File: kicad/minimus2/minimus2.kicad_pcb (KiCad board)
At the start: 2 copper layers, 55.5 x 50 mm, 73 parts, among them J1 PROG_SER, J2 LM, J3 LM, Q1 SSM6N58NU_LF, Q2 SSM6N58NU_LF, Q3 DMN3051L, SW1 RESET, SW2 USER_A, SW3 USER_B, U1 LSM6DSRTR, U2 STM32U575CITx, U3 DRV8835, U4 AS5047D, U5 AS5047D, U6 BCR420UFD-7

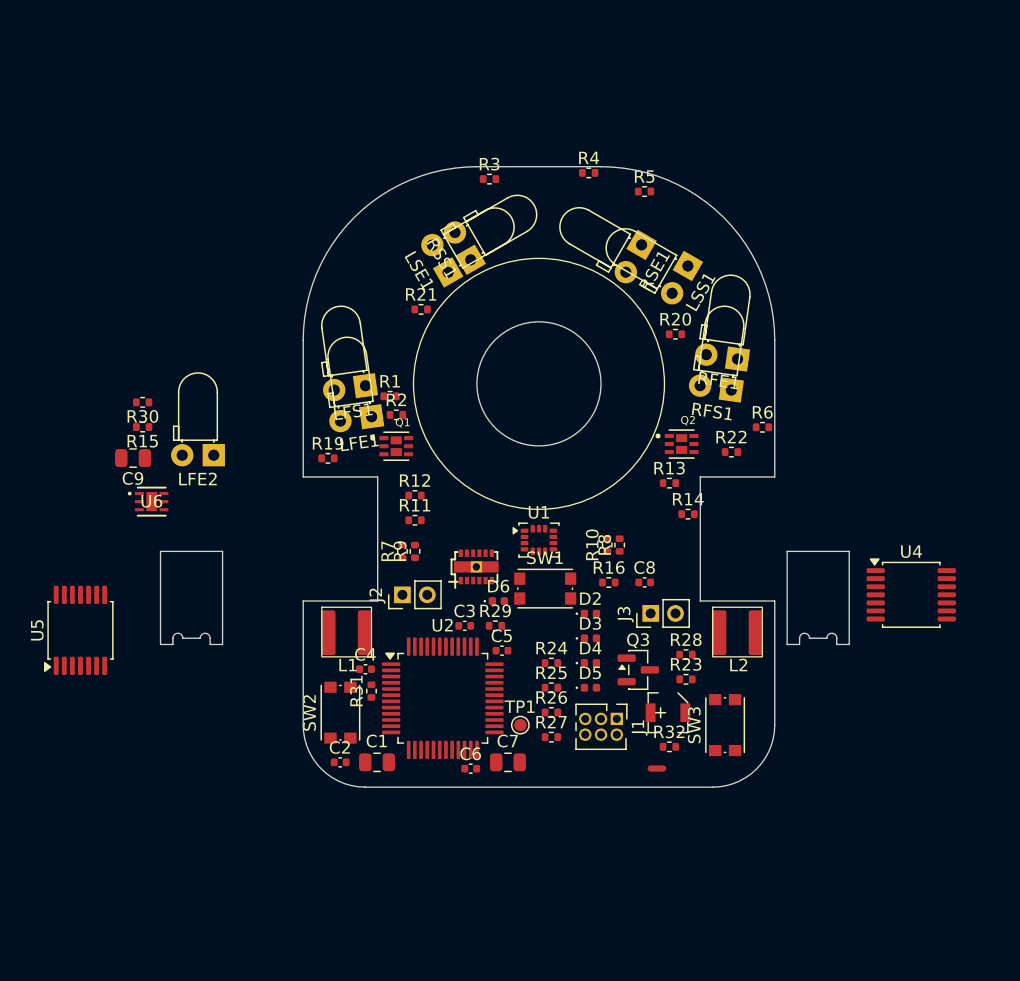
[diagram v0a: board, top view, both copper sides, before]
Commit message: remove unused switch and sensor
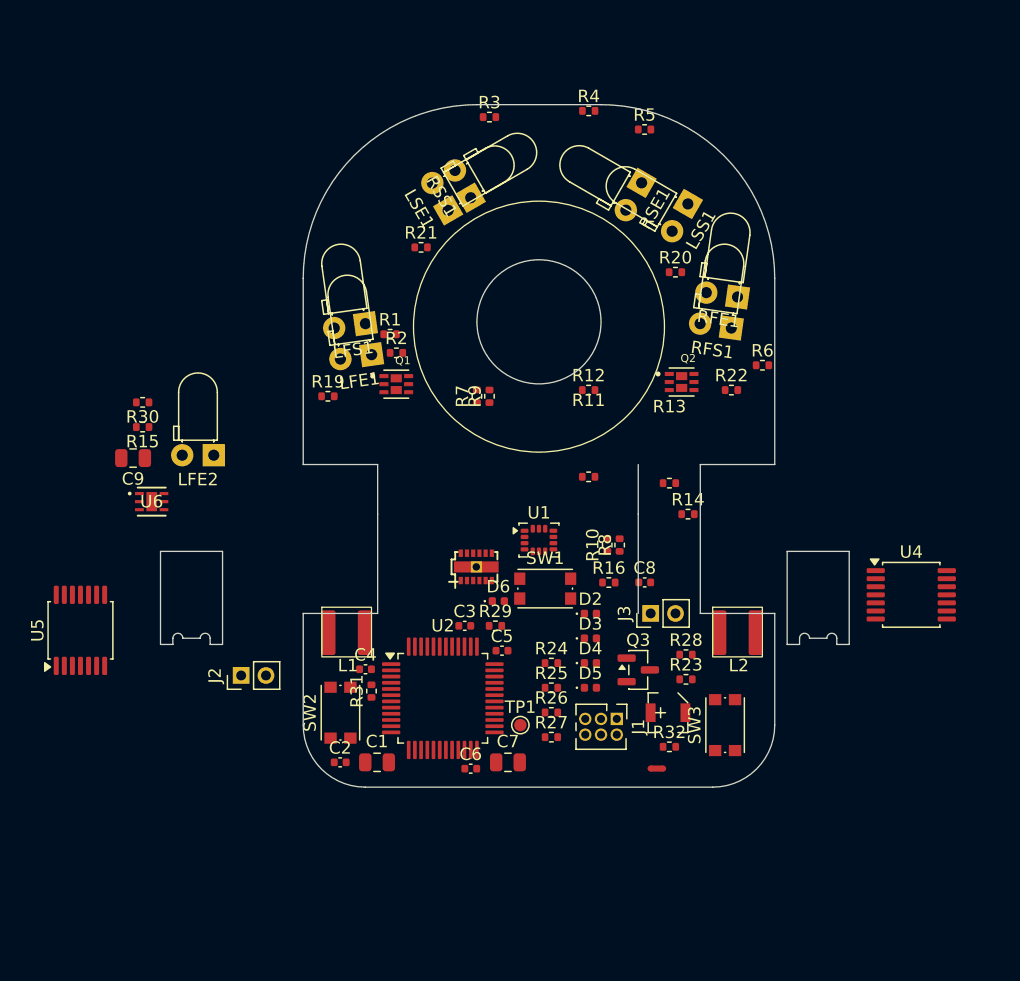
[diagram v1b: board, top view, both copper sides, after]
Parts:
- moved R12 16.4 mm to (104.0, 88.0)
- moved J2 14.5 mm to (76.0, 111.0)
- moved R11 14.4 mm to (104.0, 95.0)
- moved R7 13.9 mm to (95.0, 88.5)
- moved R9 13.9 mm to (96.0, 88.5)
- moved LFE1 5.00 mm to (86.5, 85.1)
- moved LFS1 5.00 mm to (86.0, 82.6)
- moved LSE1 5.00 mm to (92.7, 73.5)
- moved LSS1 5.00 mm to (112.0, 73.0)
- moved Q1 5.00 mm to (88.5, 87.5)
- moved Q2 5.00 mm to (111.5, 87.3)
- moved R1 5.00 mm to (88.0, 83.5)
- moved R19 5.00 mm to (83.0, 88.5)
- moved R2 5.00 mm to (88.5, 85.0)
- moved R20 5.00 mm to (111.0, 78.5)
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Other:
- board size 55.5 x 50 mm -> 55.5 x 55 mm

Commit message: add regulators and rotate board
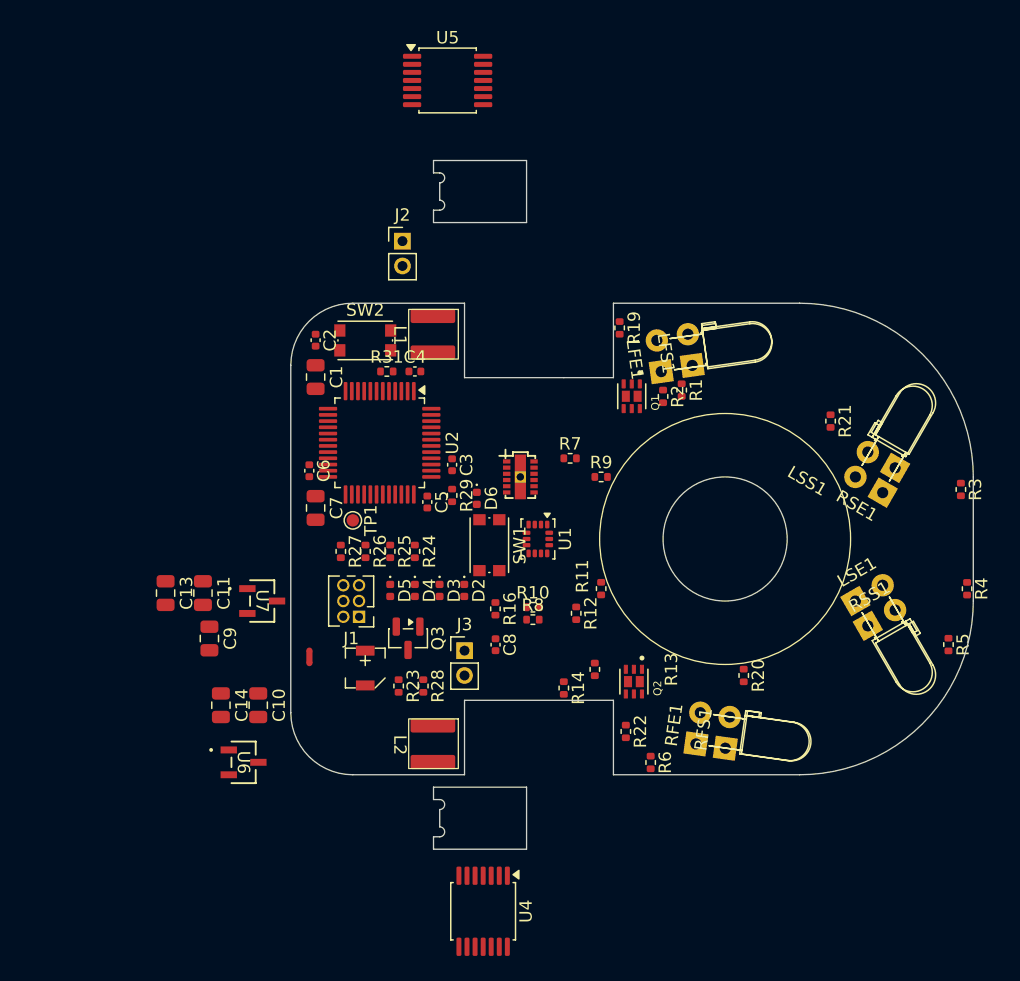
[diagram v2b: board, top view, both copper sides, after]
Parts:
- removed LFE2: SFH4050, LED_THT:LED_D3.0mm_Horizontal_O1.27mm_Z2.0mm_IRBlack
- removed R15, R30: 5k6, Resistor_SMD:R_0402_1005Metric
- removed R32: 47k, Resistor_SMD:R_0402_1005Metric
- removed SW3: USER_B, Button_Switch_SMD:SW_Push_1P1T_NO_CK_KMR2
- added C10: 4.7uF, Capacitor_SMD:C_0805_2012Metric, F.Cu at (77.4, 113.4)
- added C11: 4.7uF, Capacitor_SMD:C_0805_2012Metric, F.Cu at (72.9, 104.4)
- added C13: 4.7uF, Capacitor_SMD:C_0805_2012Metric, F.Cu at (69.9, 104.4)
- added C14: 4.7uF, Capacitor_SMD:C_0805_2012Metric, F.Cu at (74.4, 113.4)
- added U7: AP2210N-3.3TRG1, minimus:AP2210N-x.xTRG1_DIO, F.Cu at (77.7, 105.0)
- LFE1, LSE1, RFE1, RSE1: footprint LED_THT:LED_D3.0mm_Horizontal_O1.27mm_Z2.0mm_IRBlack -> LED_THT:LED_D3.0mm_Horizontal_O3.81mm_Z6.0mm
- U6: value BCR420UFD-7 -> AP2210N-5.0TRG1; footprint BCR420UFD:U-DFN2020-6_2X2_DIO -> minimus:AP2210N-x.xTRG1_DIO
- moved U5 53.3 mm to (92.6, 63.0), turned to 0 degrees
- moved R4 49.1 mm to (134.5, 104.0), turned to -90 degrees
- moved R3 48.4 mm to (134.0, 96.0), turned to -90 degrees
- moved R5 48.2 mm to (133.0, 108.5), turned to -90 degrees
- moved RSS1 47.1 mm to (126.5, 107.0), turned to 30 degrees
- moved LSE1 45.5 mm to (125.5, 105.0), turned to 30 degrees
- moved U4 42.9 mm to (95.5, 130.0), turned to -90 degrees
- moved J2 37.3 mm to (89.0, 76.0), turned to 0 degrees
- moved RFE1 36.2 mm to (112.6, 116.5), turned to 82 degrees
- moved R21 35.8 mm to (123.5, 90.5), turned to -90 degrees
- moved C2 34.1 mm to (82.0, 84.0), turned to -90 degrees
- moved RFS1 33.9 mm to (115.0, 116.9), turned to 82 degrees
- moved R6 33.3 mm to (109.0, 118.0), turned to -90 degrees
- moved R20 33.0 mm to (116.5, 111.0), turned to -90 degrees
- moved RSE1 31.6 mm to (127.7, 96.3), turned to 150 degrees
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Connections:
- net LSE renamed DS_HI
- net RFE renamed RF_ON
- net RSE renamed DS_LO
- C9 pad 1: Net-(LFE2-A) -> +5V
- R9 pad 1: LFE -> LF_ON
- U6 pad 1: unconnected-(U6-N/C-Pad1) -> GND
- U6 pad 2: Net-(LFE2-K) -> +3.3V
- U6 pad 3: unconnected-(U6-N/C-Pad3) -> +5V
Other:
- board size 55.5 x 55 mm -> 55 x 55.5 mm

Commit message: update board footprints
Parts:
- added SW4: SW_SPDT, minimus:CUS-12TB_NDC, F.Cu at (81.5, 108.4)
- LFE1, LSE1, RFE1, RSE1: footprint LED_THT:LED_D3.0mm_Horizontal_O3.81mm_Z6.0mm -> LED_THT:LED_D3.0mm_Horizontal_O1.27mm_Z2.0mm_IRBlack
